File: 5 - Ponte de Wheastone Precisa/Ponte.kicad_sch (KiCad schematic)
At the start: 26 parts, among them J1 Supply, J2 V_OUT, J3 Conn_01x02, J4 R_adj, J5 V_OUT, Q1 MMBT2222A, Q2 MMBT2222A, U1 OPA2192IDR, U2 INA333, U3 LM285D-2.5R2G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

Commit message: Adicionado sensor 4 fios; PCB_1
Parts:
- removed J3: Conn_01x02, Connector_Molex:Molex_KK-254_AE-6410-02A_1x02_P2.54mm_Vertical, symbol Connector_Generic:Conn_01x02
- added C8: 0.1uF, Capacitor_SMD:C_0805_2012Metric_Pad1.18x1.45mm_HandSolder, symbol Device:C_Small
- added D1: SMF13A, Diode_SMD:D_SOD-123F, symbol Diode:1N5908
- added D2: PRTR5V0U2X, Package_TO_SOT_SMD:SOT-143, symbol Power_Protection:PRTR5V0U2X
- added J3: Sensor, Connector_Molex:Molex_KK-254_AE-6410-04A_1x04_P2.54mm_Vertical, symbol Connector_Generic:Conn_01x04
- added R2, R8: 10, Resistor_SMD:R_0805_2012Metric_Pad1.20x1.40mm_HandSolder, symbol Device:R
- added R9: 1, Resistor_SMD:R_2512_6332Metric_Pad1.40x3.35mm_HandSolder, symbol Device:R
- added U5: TI OPA192IDBVR, Package_TO_SOT_SMD:SOT-23-5, symbol Amplifier_Operational:OPA196xDBV
- RV1, RV2: footprint Potentiometer_THT:Potentiometer_Bourns_3386P_Vertical -> Potentiometer_THT:Potentiometer_Bourns_3296W_Vertical
- renumbered U5 to U1
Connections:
- net +5V: now also C8.2, D2.4 (VCC), R9.1, U5.5 (V+); no longer C9.1, U4.5 (OUT)
- net GND: now also RV2.1, C8.1, D1.2 (A2), D2.1 (GND), U5.2 (V-); no longer RV2.3
- net at R3.2, R4.1, U1.2 (-): now also J3.1 (Pin_1); no longer U2.2 (-)
- net S+: now reaches R5.2, R6.1, RV1.1, U2.3 (+)
- net S+: now also RV2.3, D2.3 (I/O2); no longer RV2.1
- net at J2.1, J5.1 (Pin_1): now also U5.1, U5.4 (-); no longer U2.6
- net at Q1.2 (E), R3.1: now also J3.4 (Pin_4); no longer U1.5 (+)
- net at Q2.1 (B): now also R2.1; no longer U1.7
- net at C4.1, C5.1, J1.2 (Pin_2)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: now also D1.1 (A1)
- new net: R8.1, U2.6
- new net: C9.1, R9.2, U4.5 (OUT)
- new net: R2.2, U1.7
- new net: J3.3 (Pin_3), U1.5 (+)
- new net: R8.2, U5.3 (+)
- new net S-: D2.2 (I/O1), J3.2 (Pin_2), U2.2 (-)
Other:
- note added: "Para bancada/lab: Phoenix Contact ou blocos de parafuso com proteção contra vibração J3"
- note added: "adicionar um TVS"
- note removed: "Adicionar um regulador de 5V linear"
- moved on the sheet: C4, J1, J2, J5, R3, RV2

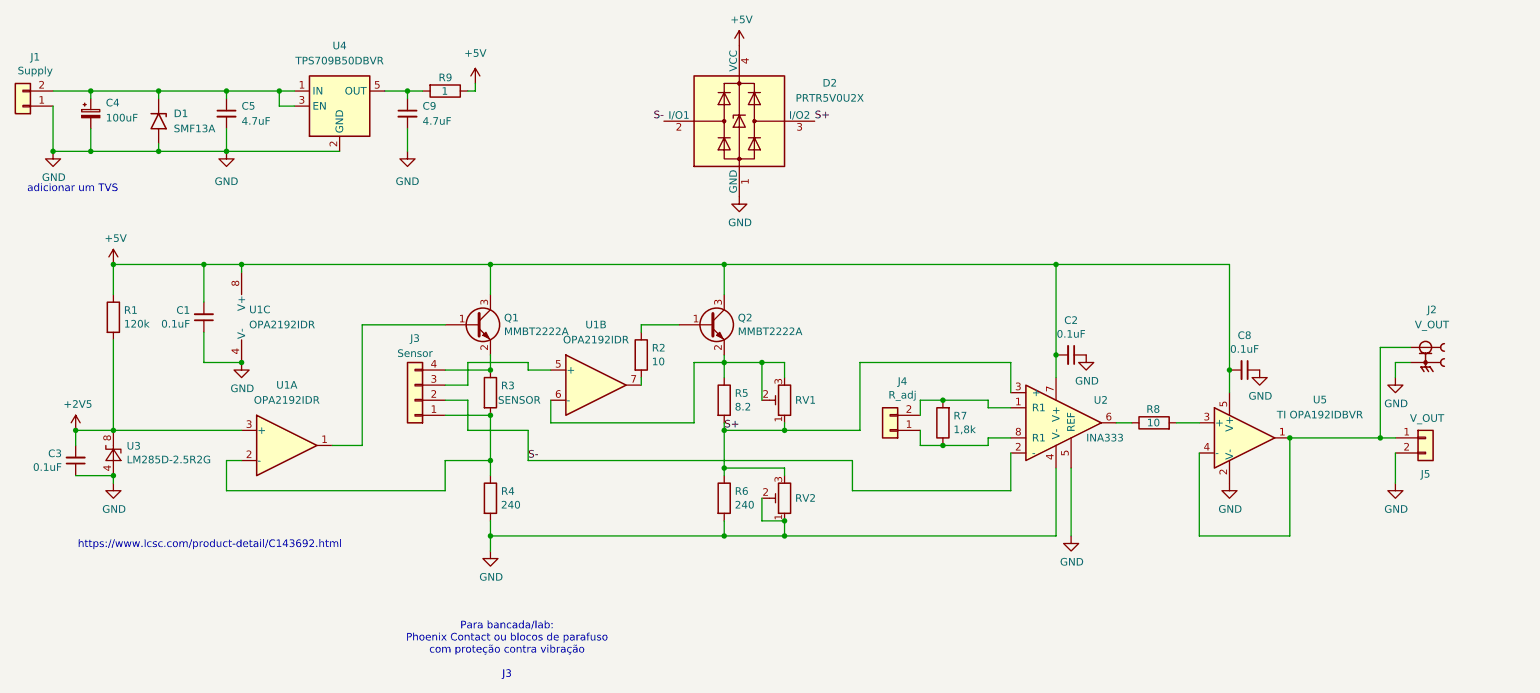
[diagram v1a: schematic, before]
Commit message: Posicionado e roteado. Restando adicionar vias de GND e guard ring.
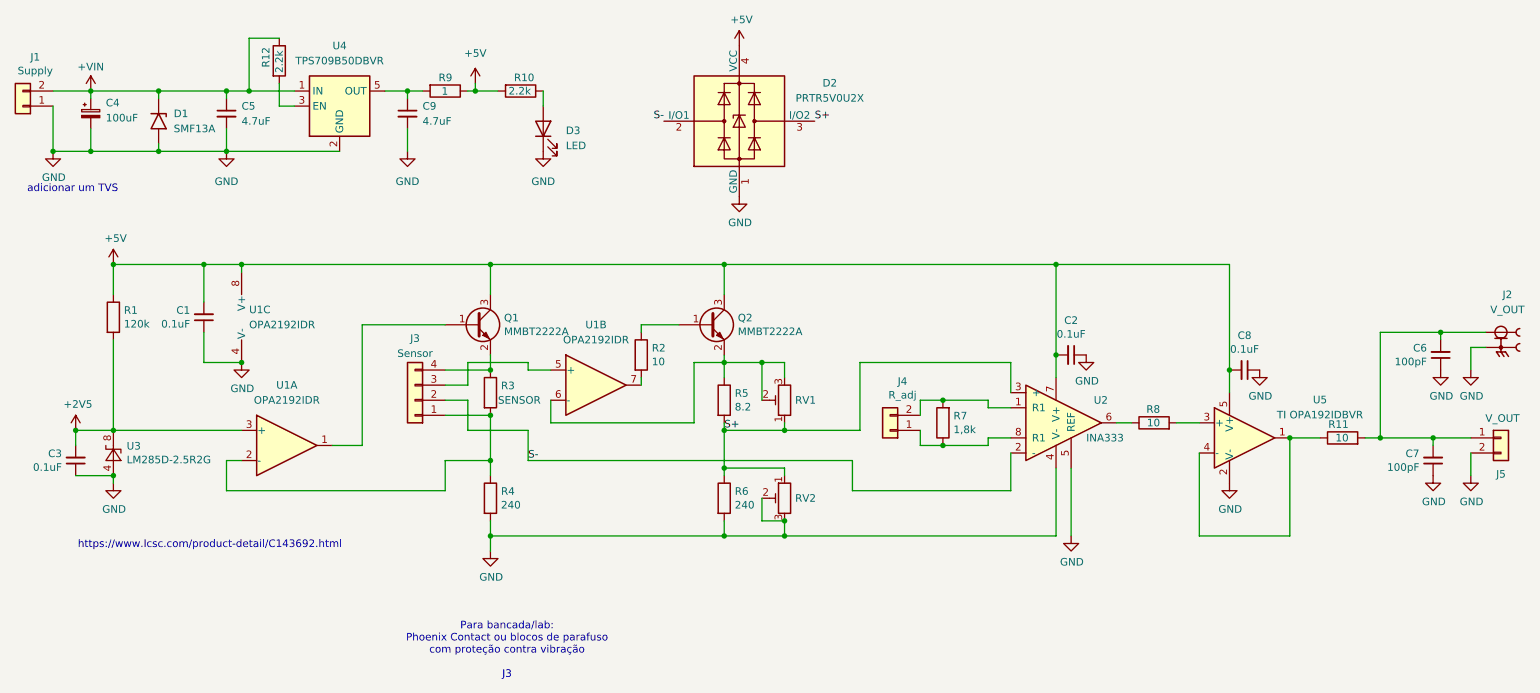
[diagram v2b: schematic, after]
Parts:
- added C6, C7: 100pF, Capacitor_SMD:C_0805_2012Metric_Pad1.18x1.45mm_HandSolder, symbol Device:C_Small
- added D3: LED, LED_SMD:LED_0805_2012Metric, symbol Device:LED
- added R10, R12: 2.2k, Resistor_SMD:R_0805_2012Metric, symbol Device:R
- added R11: 10, Resistor_SMD:R_0805_2012Metric_Pad1.20x1.40mm_HandSolder, symbol Device:R
- J4: footprint Connector_PinHeader_2.54mm:PinHeader_1x02_P2.54mm_Vertical -> Connector_Molex:Molex_KK-254_AE-6410-02A_1x02_P2.54mm_Vertical; LCSC part # C5383111 -> C5447965
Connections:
- net +5V: now also R10.2
- net GND: now also RV2.3, C6.1, C7.1, D3.1 (K); no longer RV2.1
- net S+: now also RV2.1; no longer RV2.3
- net +VIN: now reaches C4.1, C5.1, D1.1 (A1), J1.2 (Pin_2), U4.1 (IN)
- net +VIN: now also R12.1; no longer U4.3 (EN)
- net at J2.1, J5.1 (Pin_1): now also C6.2, C7.2, R11.2; no longer U5.1, U5.4 (-)
- new net: D3.2 (A), R10.1
- new net: R12.2, U4.3 (EN)
- new net: R11.1, U5.1, U5.4 (-)
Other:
- moved on the sheet: J2, J5, RV2

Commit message: Adicionado silks e furos para suporte. Preço com montagem R04,54
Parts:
- C1, C2, C3: footprint Capacitor_SMD:C_0805_2012Metric_Pad1.15x1.40mm_HandSolder -> Capacitor_SMD:C_0805_2012Metric_Pad1.18x1.45mm_HandSolder; Supplier (none) -> LCSC
- C8, J1, J4, J5, Q1, Q2, RV1, RV2: Supplier (none) -> LCSC
- D1: Supplier https://www.lcsc.com/product-detail/C2857274.html -> LCSC
- R1, R3, R4, R5, R6, R7: footprint Resistor_SMD:R_0805_2012Metric_Pad1.15x1.40mm_HandSolder -> Resistor_SMD:R_0805_2012Metric_Pad1.20x1.40mm_HandSolder; Supplier (none) -> LCSC
- R10, R12: LCSC part # LCSC -> C19269962; Supplier C19269962 -> LCSC
- R9: LCSC part # LCSC -> C4033338; Supplier C4033338 -> LCSC
- U2: footprint Package_SO:VSSOP-8_3.0x3.0mm_P0.65mm -> Package_SO:VSSOP-8_3x3mm_P0.65mm; Supplier (none) -> LCSC
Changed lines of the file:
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@@
 			)
 		)
-		(property "Footprint" "Package_SO:VSSOP-8_3.0x3.0mm_P0.65mm"
+		(property "Footprint" "Package_SO:VSSOP-8_3x3mm_P0.65mm"
 			(at 200.66 82.55 0)
 			(effects
@@
 			)
 		)
+		(property "Supplier" "LCSC"
+			(at 194.31 85.09 0)
+			(effects
+				(font
+					(size 1.27 1.27)
+				)
+				(hide yes)
+			)
+		)
 		(pin "6"
 		)
@@
 			)
 		)
-		(property "Footprint" "Resistor_SMD:R_0805_2012Metric_Pad1.15x1.40mm_HandSolder"
+		(property "Footprint" "Resistor_SMD:R_0805_2012Metric_Pad1.20x1.40mm_HandSolder"
 			(at 97.282 81.28 90)
 			(effects
@@
 			)
 		)
+		(property "Supplier" "LCSC"
+			(at 99.06 81.28 0)
+			(effects
+				(font
+					(size 1.27 1.27)
+				)
+				(hide yes)
+			)
+		)
 		(pin "1"
 		)
@@
 			)
 		)
-		(property "Footprint" "Resistor_SMD:R_0805_2012Metric_Pad1.15x1.40mm_HandSolder"
+		(property "Footprint" "Resistor_SMD:R_0805_2012Metric_Pad1.20x1.40mm_HandSolder"
 			(at 97.282 99.06 90)
 			(effects
@@
 			)
 		)
+		(property "Supplier" "LCSC"
+			(at 99.06 99.06 0)
+			(effects
+				(font
+					(size 1.27 1.27)
+				)
+				(hide yes)
+			)
+		)
 		(pin "1"
 		)
@@
 			)
 		)
-		(property "Footprint" "Resistor_SMD:R_0805_2012Metric_Pad1.15x1.40mm_HandSolder"
+		(property "Footprint" "Resistor_SMD:R_0805_2012Metric_Pad1.20x1.40mm_HandSolder"
 			(at 136.652 82.55 90)
 			(effects
@@
 			)
 		)
+		(property "Supplier" "LCSC"
+			(at 138.43 82.55 0)
+			(effects
+				(font
+					(size 1.27 1.27)
+				)
+				(hide yes)
+			)
+		)
 		(pin "1"
 		)
@@
 			)
 		)
-		(property "Footprint" "Resistor_SMD:R_0805_2012Metric_Pad1.15x1.40mm_HandSolder"
+		(property "Footprint" "Resistor_SMD:R_0805_2012Metric_Pad1.20x1.40mm_HandSolder"
 			(at 136.652 99.06 90)
 			(effects
@@
 			)
 		)
+		(property "Supplier" "LCSC"
+			(at 138.43 99.06 0)
+			(effects
+				(font
+					(size 1.27 1.27)
+				)
+				(hide yes)
+			)
+		)
 		(pin "1"
 		)
@@
 			)
 		)
+		(property "Supplier" "LCSC"
+			(at 96.52 69.85 0)
+			(effects
+				(font
+					(size 1.27 1.27)
+				)
+				(hide yes)
+			)
+		)
 		(pin "2"
 		)
@@
 			)
 		)
+		(property "Supplier" "LCSC"
+			(at 135.89 69.85 0)
+			(effects
+				(font
+					(size 1.27 1.27)
+				)
+				(hide yes)
+			)
+		)
 		(pin "2"
 		)
@@
 			)
 		)
-		(property "Footprint" "Resistor_SMD:R_0805_2012Metric_Pad1.15x1.40mm_HandSolder"
+		(property "Footprint" "Resistor_SMD:R_0805_2012Metric_Pad1.20x1.40mm_HandSolder"
 			(at 177.038 86.36 90)
 			(effects
@@
 			)
 		)
+		(property "Supplier" "LCSC"
+			(at 175.26 86.36 0)
+			(effects
+				(font
+					(size 1.27 1.27)
+				)
+				(hide yes)
+			)
+		)
 		(pin "1"
 		)
@@
 			)
 		)
-		(property "Supplier" ""
+		(property "Supplier" "LCSC"
 			(at 148.59 82.55 0)
 			(effects
@@
 			)
 		)
-		(property "Supplier" ""
+		(property "Supplier" "LCSC"
 			(at 148.59 99.06 0)
 			(effects
@@
 			)
 		)
-		(property "Supplier" ""
+		(property "Supplier" "LCSC"
 			(at 166.37 87.63 0)
 			(effects
@@
 			)
 		)
-		(property "Footprint" "Capacitor_SMD:C_0805_2012Metric_Pad1.15x1.40mm_HandSolder"
+		(property "Footprint" "Capacitor_SMD:C_0805_2012Metric_Pad1.18x1.45mm_HandSolder"
 			(at 29.21 92.71 0)
 			(effects
@@
 			)
 		)
+		(property "Supplier" "LCSC"
+			(at 29.21 92.71 0)
+			(effects
+				(font
+					(size 1.27 1.27)
+				)
+				(hide yes)
+			)
+		)
 		(pin "1"
 		)
@@
 			)
 		)
-		(property "Supplier" ""
+		(property "Supplier" "LCSC"
 			(at 20.32 33.02 0)
 			(effects
@@
 			)
 		)
+		(property "Supplier" "LCSC"
+			(at 269.24 88.9 0)
+			(effects
+				(font
+					(size 1.27 1.27)
+				)
+				(hide yes)
+			)
+		)
 		(pin "1"
 		)
@@
 			)
 		)
-		(property "Footprint" "Capacitor_SMD:C_0805_2012Metric_Pad1.15x1.40mm_HandSolder"
+		(property "Footprint" "Capacitor_SMD:C_0805_2012Metric_Pad1.18x1.45mm_HandSolder"
 			(at 196.85 74.93 0)
 			(effects
@@
 			)
 		)
+		(property "Supplier" "LCSC"
+			(at 196.85 74.93 90)
+			(effects
+				(font
+					(size 1.27 1.27)
+				)
+				(hide yes)
+			)
+		)
 		(pin "2"
 		)
@@
 			)
 		)
-		(property "Footprint" "Capacitor_SMD:C_0805_2012Metric_Pad1.15x1.40mm_HandSolder"
+		(property "Footprint" "Capacitor_SMD:C_0805_2012Metric_Pad1.18x1.45mm_HandSolder"
 			(at 50.8 68.58 0)
 			(effects
@@
 			)
 		)
-		(property "Supplier" ""
+		(property "Supplier" "LCSC"
 			(at 50.8 68.58 0)
 			(effects
@@
 			)
 		)
-		(property "Footprint" "Resistor_SMD:R_0805_2012Metric_Pad1.15x1.40mm_HandSolder"
+		(property "Footprint" "Resistor_SMD:R_0805_2012Metric_Pad1.20x1.40mm_HandSolder"
 			(at 33.782 68.58 90)
 			(effects
@@
 			)
 		)
+		(property "Supplier" "LCSC"
+			(at 35.56 68.58 0)
+			(effects
+				(font
+					(size 1.27 1.27)
+				)
+				(hide yes)
+			)
+		)
 		(pin "1"
 		)
@@
 			)
 		)
-		(property "LCSC part #" "LCSC"
+		(property "LCSC part #" "C19269962"
 			(at 63.5 25.4 0)
 			(effects
@@
 			)
 		)
-		(property "Supplier" "C19269962"
+		(property "Supplier" "LCSC"
 			(at 63.5 25.4 0)
 			(effects
@@
 			)
 		)
-		(property "Supplier" ""
+		(property "Supplier" "LCSC"
 			(at 226.06 77.47 0)
 			(effects
@@
 			)
 		)
-		(property "Supplier" "https://www.lcsc.com/product-detail/C2857274.html"
+		(property "Supplier" "LCSC"
 			(at 43.18 35.56 0)
 			(effects
@@
 			)
 		)
-		(property "LCSC part #" "LCSC"
+		(property "LCSC part #" "C4033338"
 			(at 91.44 30.48 0)
 			(effects
@@
 			)
 		)
-		(property "Supplier" "C4033338"
+		(property "Supplier" "LCSC"
 			(at 91.44 30.48 0)
 			(effects
@@
 			)
 		)
-		(property "LCSC part #" "LCSC"
+		(property "LCSC part #" "C19269962"
 			(at 104.14 30.48 0)
 			(effects
@@
 			)
 		)
-		(property "Supplier" "C19269962"
+		(property "Supplier" "LCSC"
 			(at 104.14 30.48 0)
 			(effects
